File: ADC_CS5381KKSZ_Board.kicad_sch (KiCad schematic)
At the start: 87 parts, among them IC1 OpAmp_NE5532D, J1 Mode_Selection_Jumpers, J13 MCLK_DIV_Jumper, J14 JST_XH_2.54_Plug_5V+, J15 USB_B_Micro, J16 USB_D_Jumper, J17 MCLK_Jumper, J2 I2S_OR_LJ_OUT, J3 I/O_Headers_1, J5 I/O_Headers_2, J6 I2S_OR_LJ_OUT, J7 I2S_OR_LJ_OUT, J8 HP_FILTER_EN, Q2 MOSFET_SI2333DDS-T1-BE3, U1 CS5381

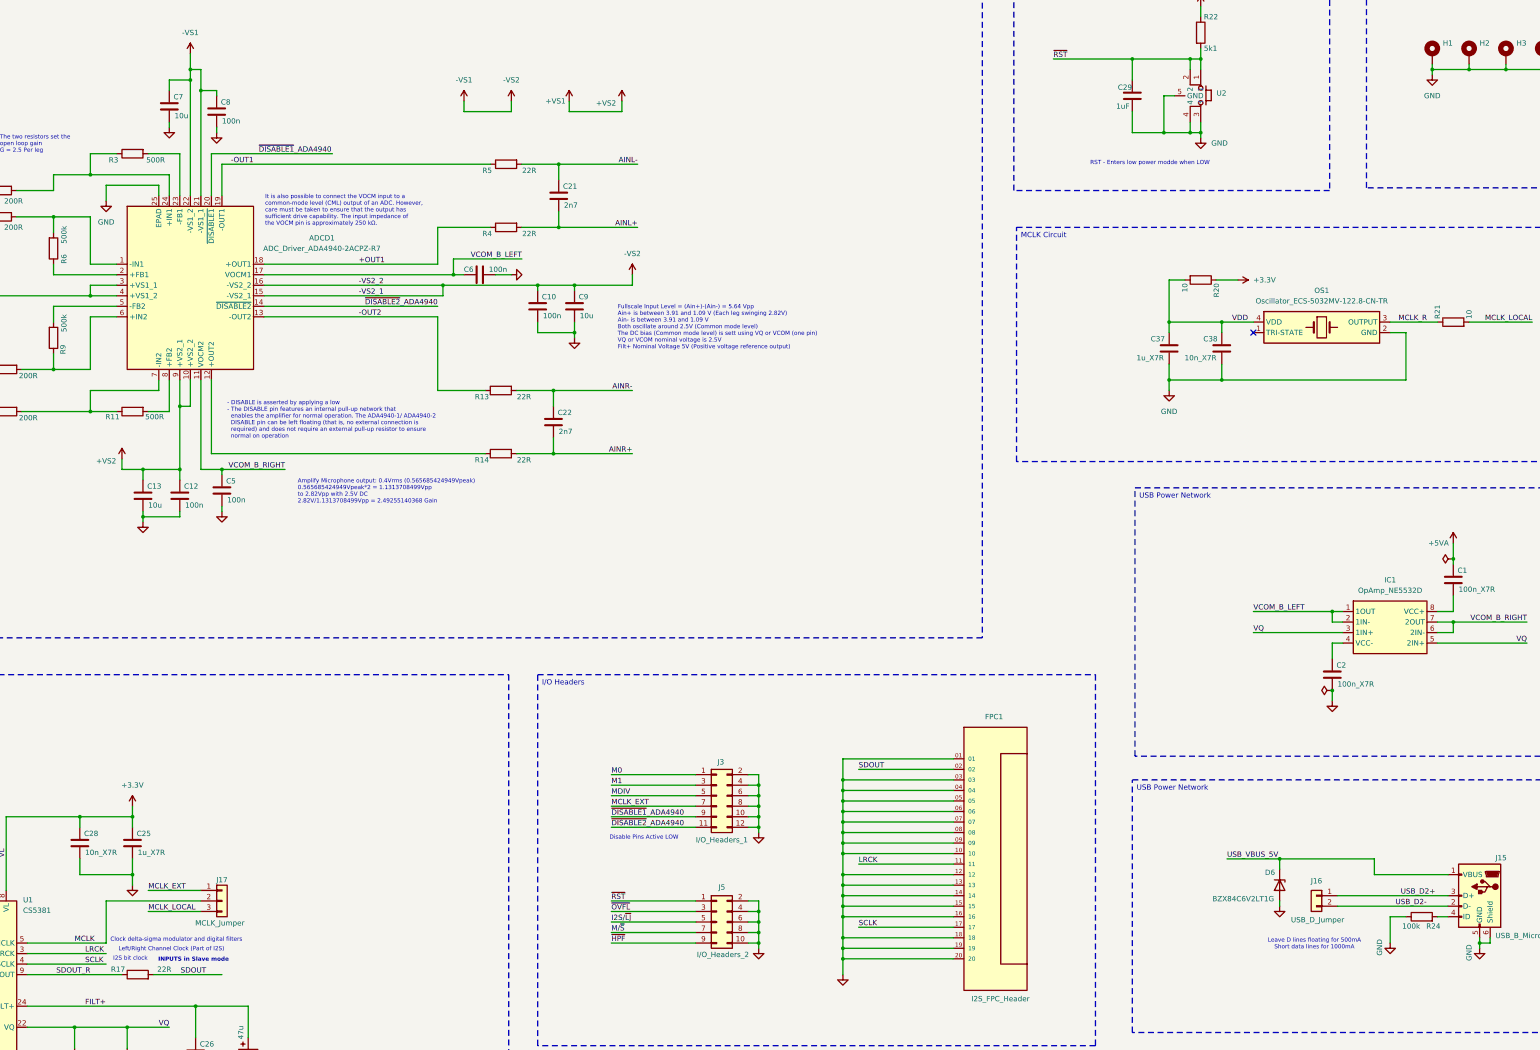
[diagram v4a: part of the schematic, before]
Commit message: Update ADC_CS5381KKSZ_Board.kicad_sch
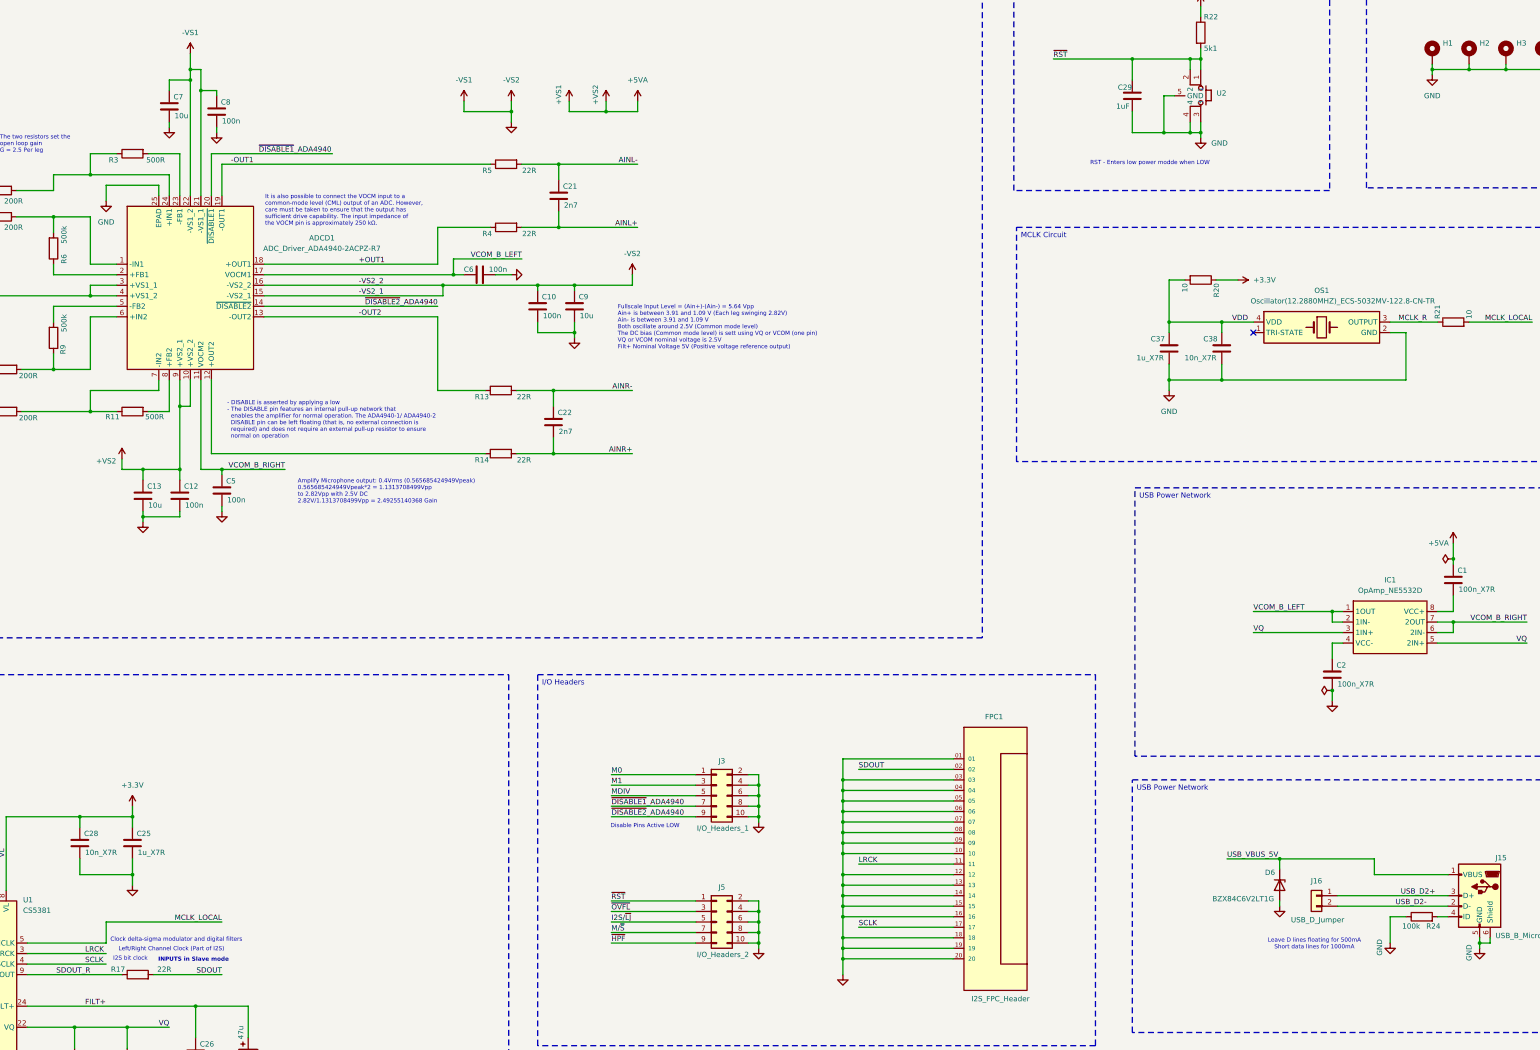
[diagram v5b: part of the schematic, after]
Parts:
- removed J17: MCLK_Jumper, Connector_PinHeader_2.54mm:PinHeader_1x03_P2.54mm_Vertical, symbol Connector_Generic:Conn_01x03
- removed J3: I/O_Headers_1, symbol Connector_Generic:Conn_02x06_Odd_Even
- added J3: I/O_Headers_1, Connector_PinHeader_2.54mm:PinHeader_2x05_P2.54mm_Horizontal, symbol Connector_Generic:Conn_02x05_Odd_Even
- OS1: value Oscillator_ECS-5032MV-122.8-CN-TR -> Oscillator(12.2880MHZ)_ECS-5032MV-122.8-CN-TR
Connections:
- net +VS1 is gone; now on net +5VA: ADCD1.10 (+VS2_2), ADCD1.3 (+VS1_1), ADCD1.4 (+VS1_2), ADCD1.9 (+VS2_1), C11.1, C12.1, C13.1, C14.1
- net GND is gone; now on net -VS1: ADCD1.25 (EPAD), C10.2, C11.2, C12.2, C13.2, C14.2, C17.2, C18.2, C2.2, C23.2, C24.2, C25.2, C26.2, C27.2, C28.2, C29.1, C3.2, C30.2, C31.2, C33.2, C34.2, C35.2, C36.2, C37.2, C38.2, C4.2, C5.2, C6.2, C7.2, C8.2, C9.2, D3.1 (A), D6.1 (A), FPC1.01, FPC1.03, FPC1.04, FPC1.05, FPC1.06, FPC1.07, FPC1.08, FPC1.09, FPC1.10, FPC1.12, FPC1.13, FPC1.14, FPC1.15, FPC1.16, FPC1.18, FPC1.19, FPC1.20, H1.1, H2.1, H3.1, H4.1, J1.5 (Pin_5), J1.6 (Pin_6), J13.3 (Pin_3), J14.1 (POWER-), J15.5 (GND), J15.6 (Shield), J5.10 (Pin_10), J5.2 (Pin_2), J5.4 (Pin_4), J5.6 (Pin_6), J5.8 (Pin_8), J6.3 (Pin_3), J7.3 (Pin_3), J8.3 (Pin_3), LDO1.2 (GND), MK1.4 (GND), MK3.4 (GND), OS1.2 (GND), R23.2, R24.1, U1.18 (GND), U1.23 (REFGND), U1.7 (GND), U2.3, U2.4, U2.5 (GND)
- net MCLK is gone; now on net MCLK_LOCAL: U1.5 (MCLK)
- net -VS1: now also J3.10 (Pin_10), J3.2 (Pin_2), J3.4 (Pin_4), J3.6 (Pin_6), J3.8 (Pin_8)
- net M0: now also J3.1 (Pin_1)
- net M1: now also J3.3 (Pin_3)
- net MDIV: now also J3.5 (Pin_5)
- net ~{DISABLE1}_ADA4940: now also J3.7 (Pin_7)
- net ~{DISABLE2}_ADA4940: now also J3.9 (Pin_9)

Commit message: Update
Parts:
- removed C10, C8: 100n, Capacitor_SMD:C_0805_2012Metric, symbol Device:C
- removed C2: 100n_X7R, Capacitor_SMD:C_0805_2012Metric, symbol Device:C
- removed C7, C9: 10u, Capacitor_SMD:C_0805_2012Metric, symbol Device:C
- removed D3, D6: BZX84C6V2LT1G, Package_TO_SOT_SMD:SOT-23, symbol Diode:BZX84Cxx
- added Z1, Z3: Diode_BZX84C6V2-7-F, Personal_Project:Diode_BZX84C6V2_SOT96P240X110-3N, symbol Personal_Projects:Diode_BZX84C6V2-7-F
- J13: value MCLK_DIV_Jumper -> MCLK_DIV_JMP
- J6: value I2S_OR_LJ_OUT -> I2S_OR_LJ_OUT_JMP
- J7: value I2S_OR_LJ_OUT -> M_OR_S_JMP
- J8: value HP_FILTER_EN -> HP_FILTER_EN_JMP
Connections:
- net -VS1 is gone; now on net GND: ADCD1.15 (-VS2_1), ADCD1.16 (-VS2_2), ADCD1.21 (-VS1_1), ADCD1.22 (-VS1_2), ADCD1.25 (EPAD), C11.2, C12.2, C13.2, C14.2, C17.2, C18.2, C23.2, C24.2, C25.2, C26.2, C27.2, C28.2, C29.1, C3.2, C30.2, C31.2, C33.2, C34.2, C35.2, C36.2, C37.2, C38.2, C4.2, C5.2, C6.2, FPC1.01, FPC1.03, FPC1.04, FPC1.05, FPC1.06, FPC1.07, FPC1.08, FPC1.09, FPC1.10, FPC1.12, FPC1.13, FPC1.14, FPC1.15, FPC1.16, FPC1.18, FPC1.19, FPC1.20, H1.1, H2.1, H3.1, H4.1, J1.5 (Pin_5), J1.6 (Pin_6), J13.3 (Pin_3), J14.1 (POWER-), J15.5 (GND), J15.6 (Shield), J3.10 (Pin_10), J3.2 (Pin_2), J3.4 (Pin_4), J3.6 (Pin_6), J3.8 (Pin_8), J5.10 (Pin_10), J5.2 (Pin_2), J5.4 (Pin_4), J5.6 (Pin_6), J5.8 (Pin_8), J6.3 (Pin_3), J7.3 (Pin_3), J8.3 (Pin_3), LDO1.2 (GND), MK1.4 (GND), MK3.4 (GND), OS1.2 (GND), R23.2, R24.1, U1.18 (GND), U1.23 (REFGND), U1.7 (GND), U2.3, U2.4, U2.5 (GND)
- net USB_VBUS_5V: now also Z1.3 (K)
- net MIC_L_OUTPUT+_C: now reaches C15.2, R1.1
- net +IN1: now reaches ADCD1.24 (+IN1), R1.2, R3.1
- net at C33.1, C34.1, FB1.1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: now also Z3.3 (K)
- net MIC_R_OUTPUT-_C: now reaches C20.2, R12.1
- net -IN2: now reaches ADCD1.7 (-IN2), R11.1, R12.2
- net MIC_R_OUTPUT+_C: now reaches C19.2, R10.1
- net +IN2: now reaches ADCD1.6 (+IN2), R10.2, R9.1
- net +OUT2: now reaches ADCD1.12 (+OUT2), R14.1
- net -FB2: now reaches ADCD1.5 (-FB2), R9.2
- net GND: now reaches IC1.4 (VCC-)
- net GND: now also Z1.1 (A), Z3.1 (A)
- net +FB1: now reaches ADCD1.2 (+FB1), R6.1
- net -IN1: now reaches ADCD1.1 (-IN1), R6.2, R7.2
- net -FB1: now reaches ADCD1.23 (-FB1), R3.2
- net +FB2: now reaches ADCD1.8 (+FB2), R11.2
- net MIC_L_OUTPUT-_C: now reaches C16.2, R7.1
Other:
- note added: "1% Tolerance Resistors"
- moved on the sheet: J15, J16, R24

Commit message: Update
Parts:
- removed ADCD1: ADC_Driver_ADA4940-2ACPZ-R7, Personal_Project:ADC_Driver_ADA4940-2ACPZ-R7_QFN50P400X400X80-25N-D, symbol Personal_Projects:ADC_Driver_ADA4940-2ACPZ-R7
- removed C1: 100n_X7R, Capacitor_SMD:C_0805_2012Metric, symbol Device:C
- removed C11, C13, C15, C16, C19, C20: 10u, Capacitor_SMD:C_0805_2012Metric, symbol Device:C
- removed C12, C14, C17, C18, C5, C6: 100n, Capacitor_SMD:C_0805_2012Metric, symbol Device:C
- removed C21, C22: 2n7, Capacitor_SMD:C_0805_2012Metric, symbol Device:C
- removed C23, C25, C37, C4: 1u_X7R, Capacitor_SMD:C_0805_2012Metric, symbol Device:C
- removed C24, C26, C28, C3, C34, C35, C38: 10n_X7R, Capacitor_SMD:C_0805_2012Metric, symbol Device:C
- removed C27, C33, C36: 47u, Capacitor_SMD:C_0805_2012Metric, symbol Device:C_Polarized
- removed C30, C31: 1u, Capacitor_SMD:C_0805_2012Metric, symbol Device:C
- removed FB1: BLM21PG601SN1D_0805, Capacitor_SMD:C_0805_2012Metric, symbol Device:FerriteBead
- removed FPC1: I2S_FPC_Header, Personal_Project:FPC_SAMTEC_ZF5S-20-01-T-WT, symbol Personal_Projects:FPC_ZF5S-20-01-T-WT
- removed H1, H2, H3, H4: MountingHole_Pad, MountingHole:MountingHole_3.2mm_M3_Pad, symbol Mechanical:MountingHole_Pad
- removed IC1: OpAmp_NE5532D, Personal_Project:OpAmp_NE5532DR_SOIC127P600X175-8N, symbol Personal_Projects:OpAmp_NE5532DR
- removed J1: Mode_Selection_Jumpers, Connector_PinHeader_2.54mm:PinHeader_2x03_P2.54mm_Vertical, symbol Connector_Generic:Conn_02x03_Odd_Even
- removed J13: MCLK_DIV_JMP, Connector_PinHeader_2.54mm:PinHeader_1x03_P2.54mm_Vertical, symbol Connector_Generic:Conn_01x03
- removed J14: JST_XH_2.54_Plug_5V+, Personal_Project:Connector_Power2pin_SHDRRA2W80P0X250_1X2_740X1150X610P, symbol Personal_Projects:Connector_Power2pin_JST_XH_2.54_Plug
- removed J15: USB_B_Micro, Connector_USB:USB_Micro-B_Molex-105017-0001, symbol Connector:USB_B_Micro
- removed J16: USB_D_Jumper, Connector_PinHeader_2.54mm:PinHeader_1x02_P2.54mm_Vertical, symbol Connector_Generic:Conn_01x02
- removed J2: I2S_OR_LJ_OUT, Connector_PinHeader_2.54mm:PinHeader_1x03_P2.54mm_Vertical, symbol Connector_Generic:Conn_01x03
- removed J3: I/O_Headers_1, Connector_PinHeader_2.54mm:PinHeader_2x05_P2.54mm_Horizontal, symbol Connector_Generic:Conn_02x05_Odd_Even
- removed J5: I/O_Headers_2, Connector_PinHeader_2.54mm:PinHeader_2x05_P2.54mm_Horizontal, symbol Connector_Generic:Conn_02x05_Odd_Even
- removed J6: I2S_OR_LJ_OUT_JMP, Connector_PinHeader_2.54mm:PinHeader_1x03_P2.54mm_Vertical, symbol Connector_Generic:Conn_01x03
- removed J7: M_OR_S_JMP, Connector_PinHeader_2.54mm:PinHeader_1x03_P2.54mm_Vertical, symbol Connector_Generic:Conn_01x03
- removed J8: HP_FILTER_EN_JMP, Connector_PinHeader_2.54mm:PinHeader_1x03_P2.54mm_Vertical, symbol Connector_Generic:Conn_01x03
- removed LDO1: LDO_TLV75733PDBVR, Personal_Project:LDO_SOT95P280X145-5N, symbol Personal_Projects:LDO_TLV75733PDBVR
- removed MK1, MK3: Microphone_ICS-40730, Personal_Project:Microphone_ICS40730, symbol Personal_Projects:Microphone_ICS-40730
- removed OS1: Oscillator(12.2880MHZ)_ECS-5032MV-122.8-CN-TR, Personal_Project:Oscillator_ECS5032MV250CNTR, symbol Personal_Projects:Oscillator_ECS-5032MV-122.8-CN-TR
- removed Q2: MOSFET_SI2333DDS-T1-BE3, Personal_Project:MOSFET_ SI2333DDS_SOT_DS-T1-BE3_VIS, symbol Personal_Projects:MOSFET_SI2333DDS-T1-BE3
- removed R1, R10, R12, R7: 200R, Resistor_SMD:R_0805_2012Metric, symbol Device:R
- removed R11, R3: 500R, Resistor_SMD:R_0805_2012Metric, symbol Device:R
- removed R13, R14, R17, R4, R5: 22R, Resistor_SMD:R_0805_2012Metric, symbol Device:R
- removed R20, R21: 10, Resistor_SMD:R_0805_2012Metric, symbol Device:R
- removed R23, R24: 100k, Resistor_SMD:R_0805_2012Metric, symbol Device:R
- removed R25: 10k, Resistor_SMD:R_0805_2012Metric, symbol Device:R
- removed R6, R9: 500k, Resistor_SMD:R_0805_2012Metric, symbol Device:R
- removed S1: Switch_WS-SLSU SMT Mini Slide, Personal_Project:Switch_WS-SLSU SMT Mini Slide, symbol Personal_Projects:Switch_WS-SLSU SMT Mini Slide
- removed U1: CS5381, Package_SO:SOIC-24W_7.5x15.4mm_P1.27mm, symbol Audio:CS5361
- removed Z1, Z2, Z3: Diode_BZX84C6V2-7-F, Personal_Project:Diode_BZX84C6V2_SOT96P240X110-3N, symbol Personal_Projects:Diode_BZX84C6V2-7-F
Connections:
- no-connect marks 6 -> 0
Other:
- added sheet ADC_CS5381K-KSZ (ADC_CS5381K-KSZ.kicad_sch)
- added sheet ADC_Driver_ADA4940-2ACPZ-R7 (ADC_Driver_ADA4940-2ACPZ-R7.kicad_sch)
- added sheet Interfaces (Interfaces.kicad_sch)
- added sheet Power_Management (Power_Management.kicad_sch)
- note removed: "- DISABLE is asserted by applying a low - The DISABLE pin features an internal pull-up network that enables the amplifier for normal operation. The ADA4940-1/ ADA4940-2 DISABLE pin can be left floating (that is, no external connection is required) and does not require an external pull-up resistor to ensure normal on operation"
- note removed: "1% Tolerance Resistors"
- note removed: "Amplify Microphone output: 0.4Vrms (0.565685424949Vpeak) 0.565685424949Vpeak*2 = 1.1313708499Vpp to 2.82Vpp with 2.5V DC 2.82V/1.1313708499Vpp = 2.49255140368 Gain"
- note removed: "Clock delta-sigma modulator and digital filters"
- note removed: "Disable Pins Active LOW"
- note removed: "Frequency Response from 20 Hz to 20 kHz"
- note removed: "High-pass Filter Enable"
- note removed: "I2S bit clock"
- note removed: "INPUTS in Slave mode"
- note removed: "If shutdown capability is not required, connect EN to IN."
- note removed: "Input voltage range: 5V (Exact)"
- note removed: "It is also possible to connect the VOCM input to a common-mode level (CML) output of an ADC. However, care must be taken to ensure that the output has sufficient drive capability. The input impedance of the VOCM pin is approximately 250 kΩ."
- note removed: "Leave D lines floating for 500mA Short data lines for 1000mA"
- note removed: "Left/Right Channel Clock (Part of I2S)"
- note removed: "MCLK LOW Div by 1 HIGH Div by 2"
- note removed: "Master or Slave Mode"
- note removed: "Maximum Output Voltage Single-Ended, 123 dB SPL input is 0.40V rms This is Vpp≈1.13 V."
- note removed: "ON/OFF Switch"
- note removed: "OVFL pin is open drain When no overflow detected the pin will be HIGH. When overflow detected the pin will be LOW"
- note removed: "Output DC Offset OUTPUT+ is 0.72V OUTPUT- is 0.66V"
- note removed: "Output Impedance OUTPUT+ is 180 Ohms OUTPUT- is 250 Ohms Differential is 430 Ohms"
- note removed: "Overvoltage protection for the PMOSFET VGS (VGS max is 8V)"
- note removed: "Pin 2 connects to one or three"
- note removed: "Polarity Protection"
- note removed: "Selects I2S or LJ output formats"
- note removed: "The two resistors set the open loop gain G = 2.5 Per leg"
- note removed: "To generate 3V3"
- note removed: "VA MUST BE 5V"
- note removed: "length-matched"

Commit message: Update
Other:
- sheet ADC_CS5381K-KSZ ports: added AINL+, AINL-, AINR+, AINR-, I2S/~{LJ}, LRCK, M0, M1, MDIV, M/~{S}, SCLK, SDOUT, VQ_NE5532D, ~{HPF}, ~{OVFL}, ~{RST}_CS5381; removed none
- sheet Interfaces ports: added I2S/~{LJ}, LRCK, M0, M1, MDIV, M/~{S}, SCLK, SDOUT, ~{DISABLE1}_ADA4940, ~{DISABLE2}_ADA4940, ~{HPF}, ~{OVFL}, ~{RST}_CS5381; removed none
- sheet Power_Management ports: added VCOM_B_LEFT, VCOM_B_RIGHT, VQ_NE5532D; removed none
